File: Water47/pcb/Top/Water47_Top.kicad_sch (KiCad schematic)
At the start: 4 parts

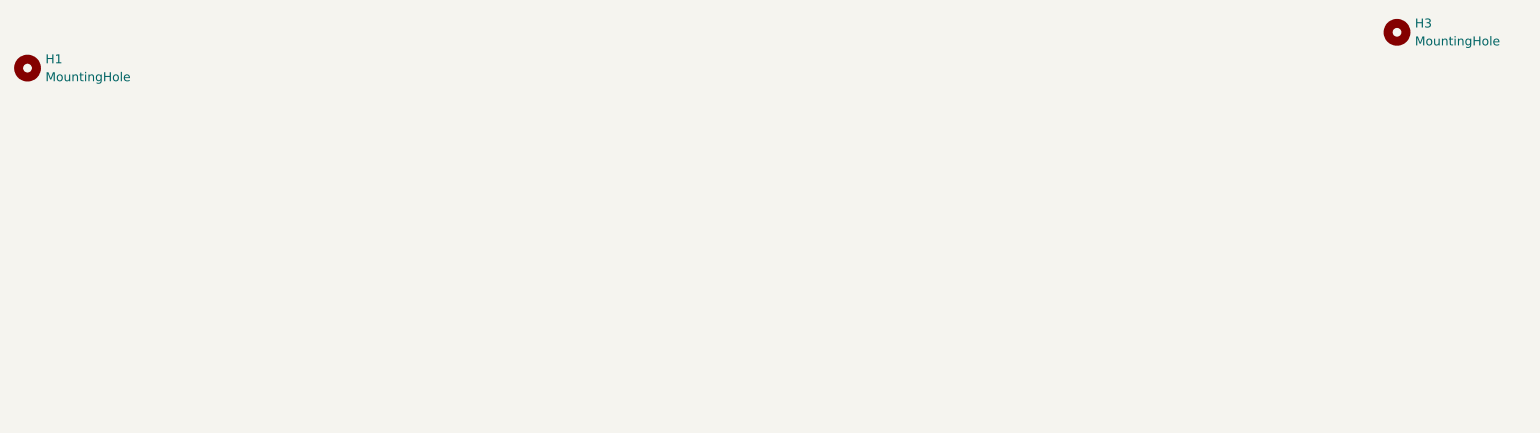
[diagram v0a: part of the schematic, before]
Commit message: feat: add mounting hole, set gerber path
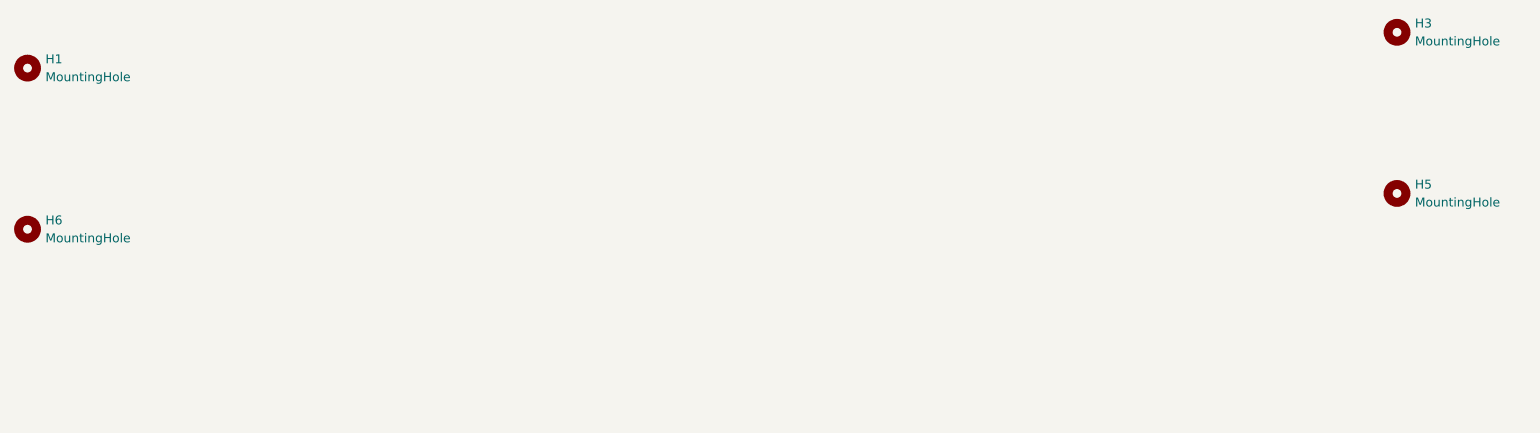
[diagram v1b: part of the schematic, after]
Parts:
- added H5, H6: MountingHole, kbd_Hole:m2_Screw_Hole, symbol Mechanical:MountingHole
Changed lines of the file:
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@@
+    )
+  )
+  (symbol (lib_id "Mechanical:MountingHole") (at 217.17 86.36 0) (unit 1)
+    (in_bom yes) (on_board yes) (fields_autoplaced)
+    (property "Reference" "H5" (id 0) (at 219.71 85.0899 0)
+      (effects (font (size 1.27 1.27)) (justify left))
+    )
+    (property "Value" "MountingHole" (id 1) (at 219.71 87.6299 0)
+      (effects (font (size 1.27 1.27)) (justify left))
+    )
+    (property "Footprint" "kbd_Hole:m2_Screw_Hole" (id 2) (at 217.17 86.36 0)
+      (effects (font (size 1.27 1.27)) hide)
+    )
+    (property "Datasheet" "~" (id 3) (at 217.17 86.36 0)
+      (effects (font (size 1.27 1.27)) hide)
     )
   )
@@
     )
     (property "Datasheet" "~" (id 3) (at 212.09 217.17 0)
+      (effects (font (size 1.27 1.27)) hide)
+    )
+  )
+  (symbol (lib_id "Mechanical:MountingHole") (at 22.86 91.44 0) (unit 1)
+    (in_bom yes) (on_board yes) (fields_autoplaced)
+    (property "Reference" "H6" (id 0) (at 25.4 90.1699 0)
+      (effects (font (size 1.27 1.27)) (justify left))
+    )
+    (property "Value" "MountingHole" (id 1) (at 25.4 92.7099 0)
+      (effects (font (size 1.27 1.27)) (justify left))
+    )
+    (property "Footprint" "kbd_Hole:m2_Screw_Hole" (id 2) (at 22.86 91.44 0)
+      (effects (font (size 1.27 1.27)) hide)
+    )
+    (property "Datasheet" "~" (id 3) (at 22.86 91.44 0)
       (effects (font (size 1.27 1.27)) hide)
     )
@@
       (reference "H4") (unit 1) (value "MountingHole") (footprint "kbd_Hole:m2_Screw_Hole")
     )
+    (path "/2c812791-8e44-4df6-bec5-ce2eb9419f11"
+      (reference "H5") (unit 1) (value "MountingHole") (footprint "kbd_Hole:m2_Screw_Hole")
+    )
+    (path "/df09d458-45fe-41b0-8cef-cc06a0cebe05"
+      (reference "H6") (unit 1) (value "MountingHole") (footprint "kbd_Hole:m2_Screw_Hole")
+    )
   )
